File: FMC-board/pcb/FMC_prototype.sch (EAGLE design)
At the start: 70 parts, among them U1 4901, U2 TPS79333, U3 ADN4663, U4 ADN4663, U5 ADN4664, U6 PDS1-S12-S5-S, U8 4901

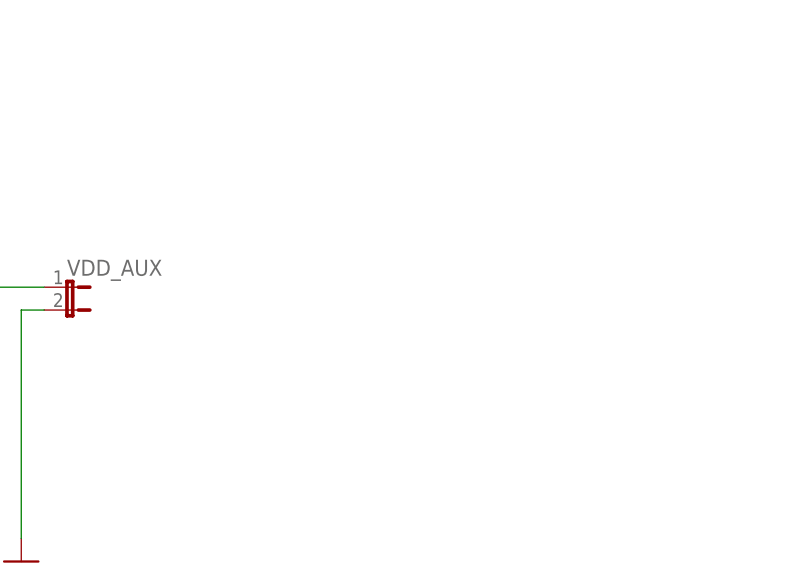
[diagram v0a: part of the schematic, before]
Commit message: tightened routing a bit & added 3v3 test point
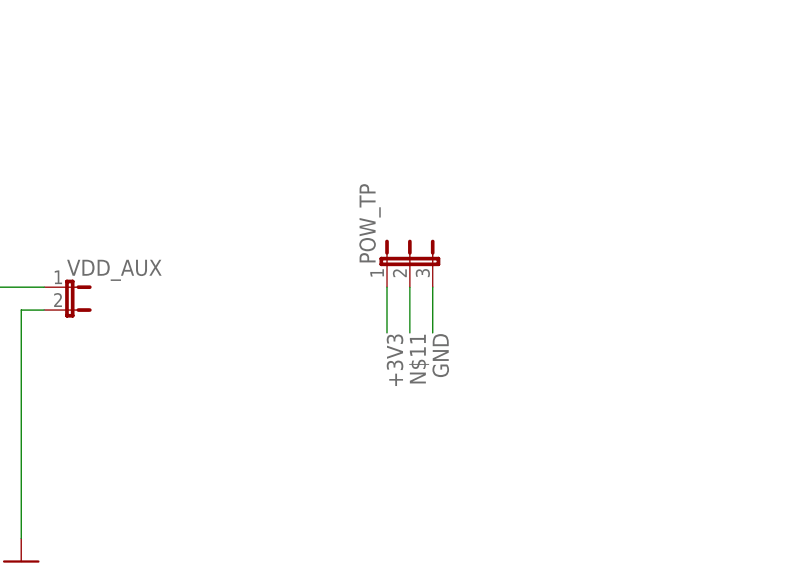
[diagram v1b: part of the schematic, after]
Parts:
- added POW_TP: (no value), jonnew:JP3E
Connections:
- new net N$11: POW_TP.2
- net +3V3: now also POW_TP.1
- net GND: now also POW_TP.3
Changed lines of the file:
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@@
 <?xml version="1.0" encoding="utf-8"?>
 <!DOCTYPE eagle SYSTEM "eagle.dtd">
-<eagle version="6.5.0">
+<eagle version="6.6.0">
 <drawing>
 <settings>
@@
 <part name="GND6" library="supply1" deviceset="GND" device=""/>
 <part name="POW_SEL" library="jonnew" deviceset="JP3E" device=""/>
+<part name="POW_TP" library="jonnew" deviceset="JP3E" device=""/>
 </parts>
 <sheets>
@@
 <instance part="GND6" gate="1" x="393.7" y="251.46"/>
 <instance part="POW_SEL" gate="G$1" x="358.14" y="370.84"/>
+<instance part="POW_TP" gate="G$1" x="452.12" y="365.76"/>
 </instances>
 <busses>
@@
 <junction x="393.7" y="256.54"/>
 </segment>
+<segment>
+<pinref part="POW_TP" gate="G$1" pin="3"/>
+<wire x1="459.74" y1="365.76" x2="459.74" y2="360.68" width="0.1524" layer="91"/>
+<label x="459.74" y="360.68" size="1.778" layer="95" rot="R270"/>
+</segment>
 </net>
 <net name="+3V3" class="0">
@@
 <pinref part="FMC" gate="G$1" pin="P$159"/>
 <wire x1="505.46" y1="66.04" x2="518.16" y2="66.04" width="0.1524" layer="91"/>
+</segment>
+<segment>
+<pinref part="POW_TP" gate="G$1" pin="1"/>
+<wire x1="454.66" y1="365.76" x2="454.66" y2="360.68" width="0.1524" layer="91"/>
+<label x="454.66" y="360.68" size="1.778" layer="95" rot="R270"/>
 </segment>
 </net>
@@
 </segment>
 </net>
+<net name="N$11" class="0">
+<segment>
+<pinref part="POW_TP" gate="G$1" pin="2"/>
+<wire x1="457.2" y1="365.76" x2="457.2" y2="360.68" width="0.1524" layer="91"/>
+<label x="457.2" y="360.68" size="1.778" layer="95" rot="R270"/>
+</segment>
+</net>

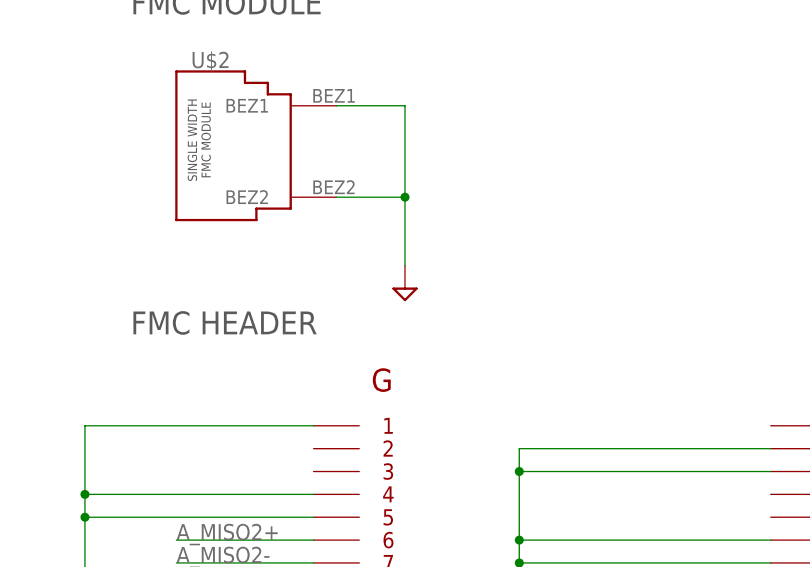
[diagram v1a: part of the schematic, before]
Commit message: connected FMC mount holes to non-isolated gnd
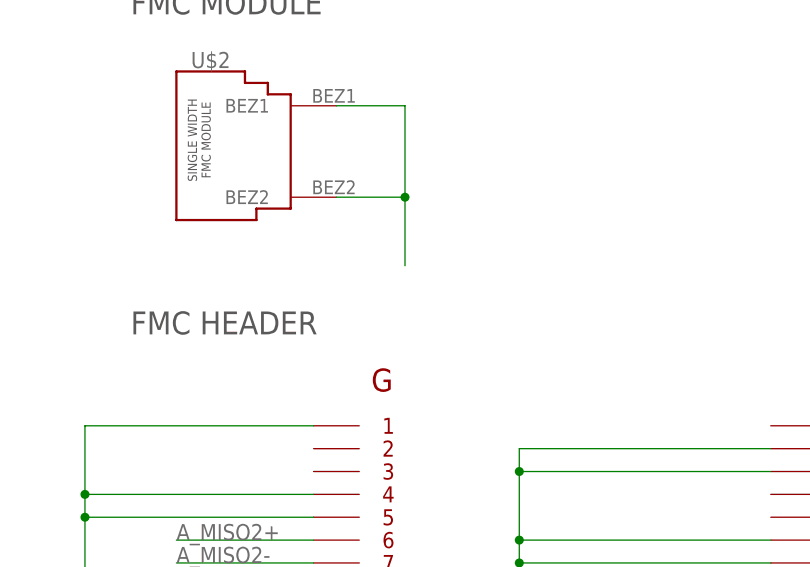
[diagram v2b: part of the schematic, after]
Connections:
- net GND: now also U$2.BEZ1, U$2.BEZ2
- net GND_ISO: no longer U$2.BEZ1, U$2.BEZ2
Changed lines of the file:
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@@
 <part name="PWR1" library="jonnew" deviceset="+3V3" device=""/>
 <part name="U$2" library="jonnew" deviceset="FMC_SINGLE_WIDTH_MODULE" device=""/>
-<part name="PWR2" library="jonnew" deviceset="GND_ISO" device=""/>
 <part name="VDD_AUX" library="jonnew" deviceset="JP2E" device="_THRU-HOLE"/>
 <part name="D4" library="jonnew" deviceset="Z-DIODE" device="_SOD-323" value="8V"/>
@@
 <instance part="PWR1" gate="PWR1" x="452.12" y="63.5" rot="R90"/>
 <instance part="U$2" gate="G$1" x="414.02" y="193.04"/>
-<instance part="PWR2" gate="G$1" x="426.72" y="180.34"/>
 <instance part="VDD_AUX" gate="G$1" x="416.56" y="365.76" rot="R270"/>
 <instance part="D4" gate="G$1" x="383.54" y="360.68" rot="R90"/>
@@
 <junction x="91.44" y="96.52"/>
 <pinref part="GND64" gate="G$1" pin="GND_ISO"/>
-</segment>
-<segment>
-<pinref part="U$2" gate="G$1" pin="BEZ2"/>
-<wire x1="419.1" y1="187.96" x2="426.72" y2="187.96" width="0.1524" layer="91"/>
-<wire x1="426.72" y1="187.96" x2="426.72" y2="180.34" width="0.1524" layer="91"/>
-<pinref part="U$2" gate="G$1" pin="BEZ1"/>
-<wire x1="419.1" y1="198.12" x2="426.72" y2="198.12" width="0.1524" layer="91"/>
-<wire x1="426.72" y1="198.12" x2="426.72" y2="187.96" width="0.1524" layer="91"/>
-<junction x="426.72" y="187.96"/>
-<pinref part="PWR2" gate="G$1" pin="GND_ISO"/>
 </segment>
 <segment>
@@
 <label x="459.74" y="360.68" size="1.778" layer="95" rot="R270"/>
 </segment>
+<segment>
+<pinref part="U$2" gate="G$1" pin="BEZ2"/>
+<wire x1="419.1" y1="187.96" x2="426.72" y2="187.96" width="0.1524" layer="91"/>
+<wire x1="426.72" y1="187.96" x2="426.72" y2="180.34" width="0.1524" layer="91"/>
+<pinref part="U$2" gate="G$1" pin="BEZ1"/>
+<wire x1="419.1" y1="198.12" x2="426.72" y2="198.12" width="0.1524" layer="91"/>
+<wire x1="426.72" y1="198.12" x2="426.72" y2="187.96" width="0.1524" layer="91"/>
+<junction x="426.72" y="187.96"/>
+</segment>
 </net>

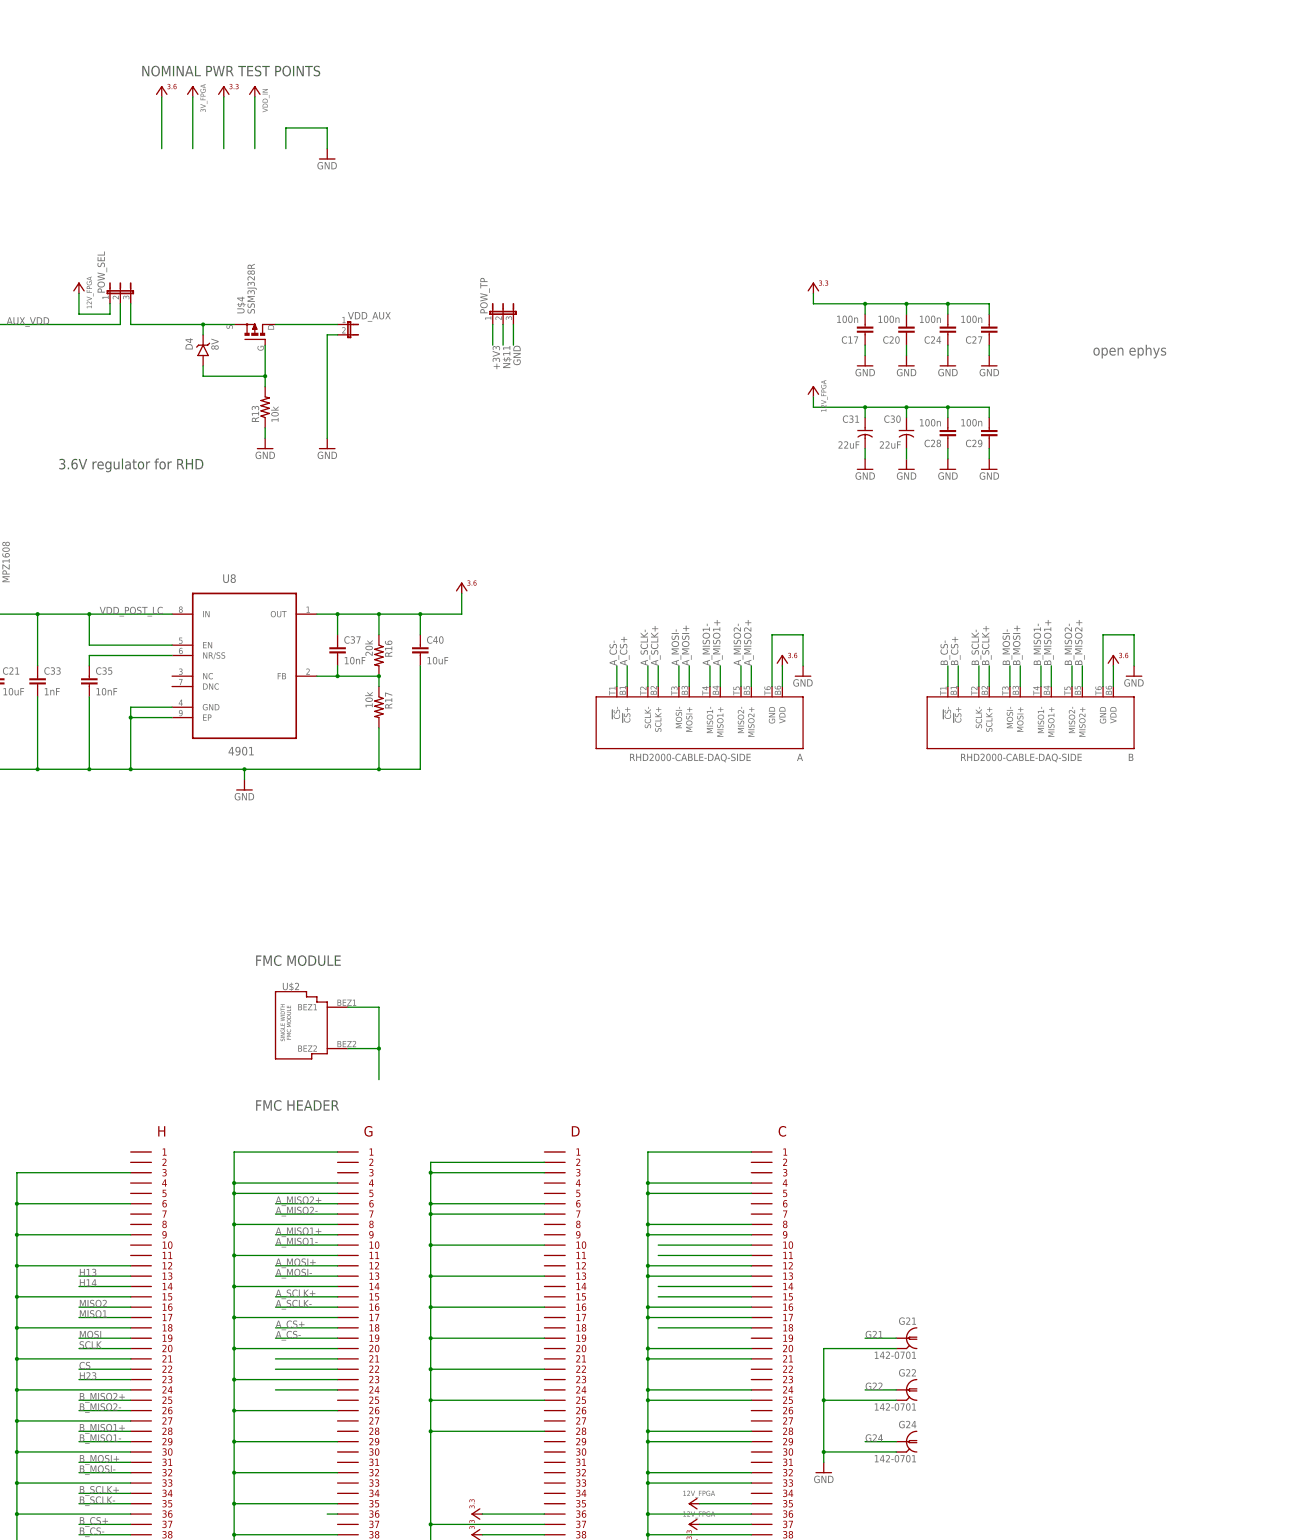
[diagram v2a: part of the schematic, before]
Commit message: added schottky diodes for FPGA input protection
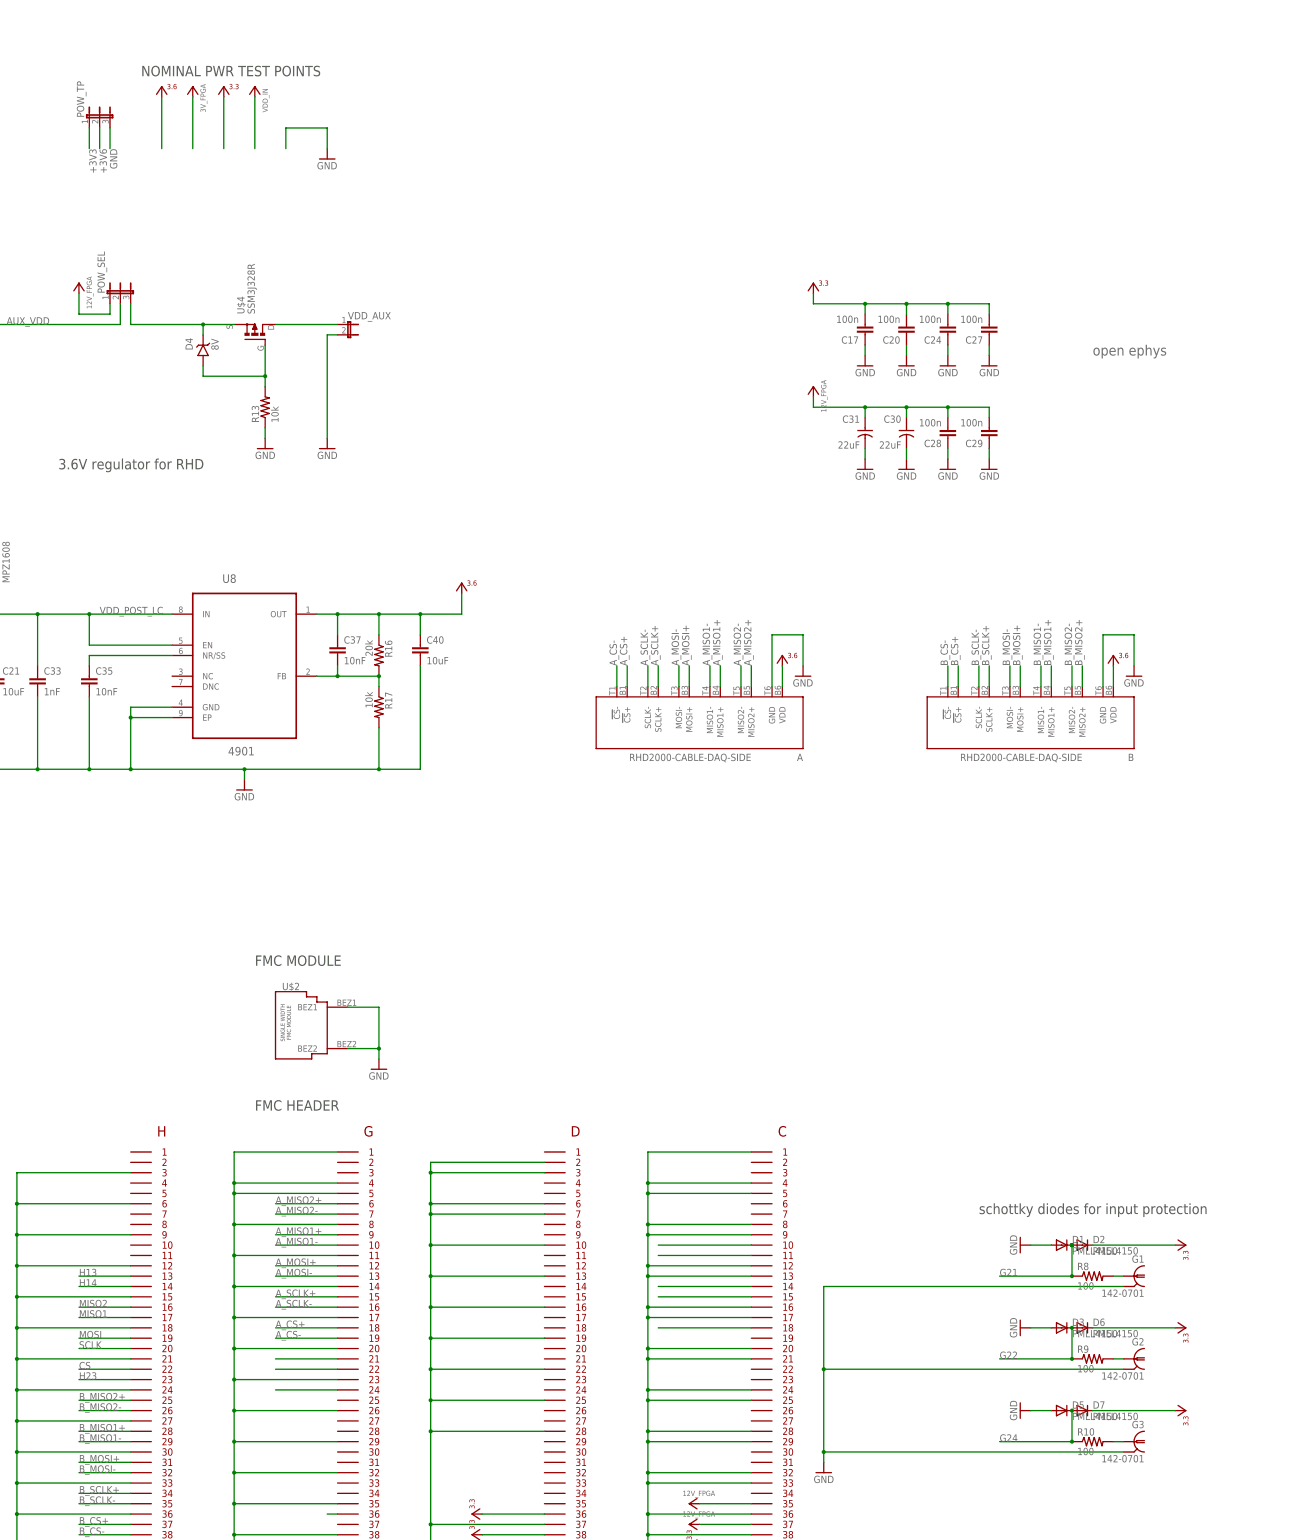
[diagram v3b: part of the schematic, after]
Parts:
- removed G21, G22, G24: 142-0701, jonnew:COAX_SMA-VERT
- added D1, D2, D3, D5, D6, D7: PMLL4150, diode:PMLL4150
- added G1, G2, G3: 142-0701, jonnew:COAX_SMA-VERT
- added R10, R8, R9: 100, jonnew:R_0603
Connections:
- removed net N$11: POW_TP.2
- new net N$18: G2.1, R9.2
- new net N$19: G3.1, R10.2
- new net N$2: G1.1, R8.2
- net +3V3: now also D2.C, D6.C, D7.C
- net +3V6: now also POW_TP.2
- net G21: now also D1.C, D2.A, R8.1; no longer G21.1
- net G22: now also D3.C, D6.A, R9.1; no longer G22.1
- net G24: now also D5.C, D7.A, R10.1; no longer G24.1
- net GND: now also D1.A, D3.A, D5.A, G1.2, G2.2, G3.2; no longer G21.2, G22.2, G24.2
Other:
- note added: "schottky diodes for input protection"
- moved on the sheet: POW_TP
